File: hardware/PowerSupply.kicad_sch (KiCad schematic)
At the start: 34 parts, among them J3 VIN+, J4 GND, Q1 RevPol, U2 LM5050-1, U3 PTPS16890VMAR, U4 LMR38020FSDDAR, U5 NCP1117ST33T3G

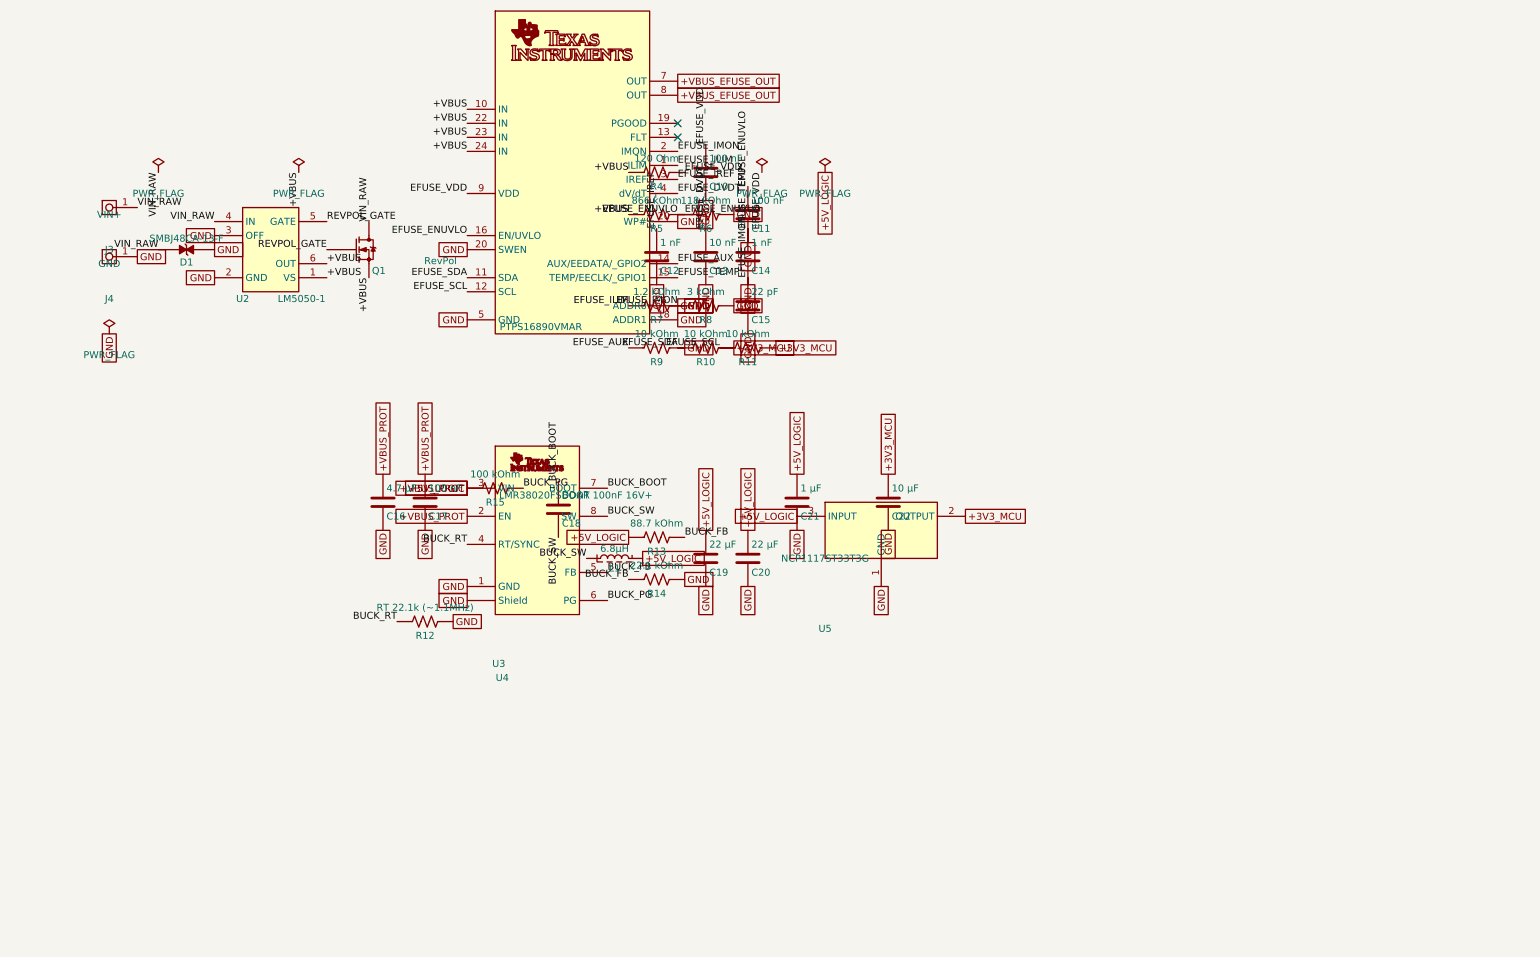
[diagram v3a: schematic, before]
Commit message: Schematic Rev B: full rebuild per METU PowerLab rules
Rev A was withdrawn: labels stuck on pins created real net shorts
(+5V_LOGIC with the 36 V bus, INHA and EFUSE_IMON with GND) and several
circuits contradicted their datasheets.

Rev B: real wires and power symbols on the 2.54 mm grid, hierarchical sheets
(half bridge reused 3x), library values, LAYOUT notes, root page with specs
and block diagram. Circuit fixes: DRV8323 VREF driven, unused buck tied to
GND, INA240A1, LM74700-Q1 reverse polarity, SMBJ36CA, eFuse per datasheet,
direct 3.3 V buck, 4.7 uH/8.1 A inductor, 2512 shunts with net-tie Kelvin,
24 V CAN ESD. kicad-cli ERC: 0 errors; netlist matches intent on all nets.
Old board and project-local library tables removed (board is rebuilt next).

Co-Authored-By: Claude Opus 5.5 <noreply@anthropic.com>
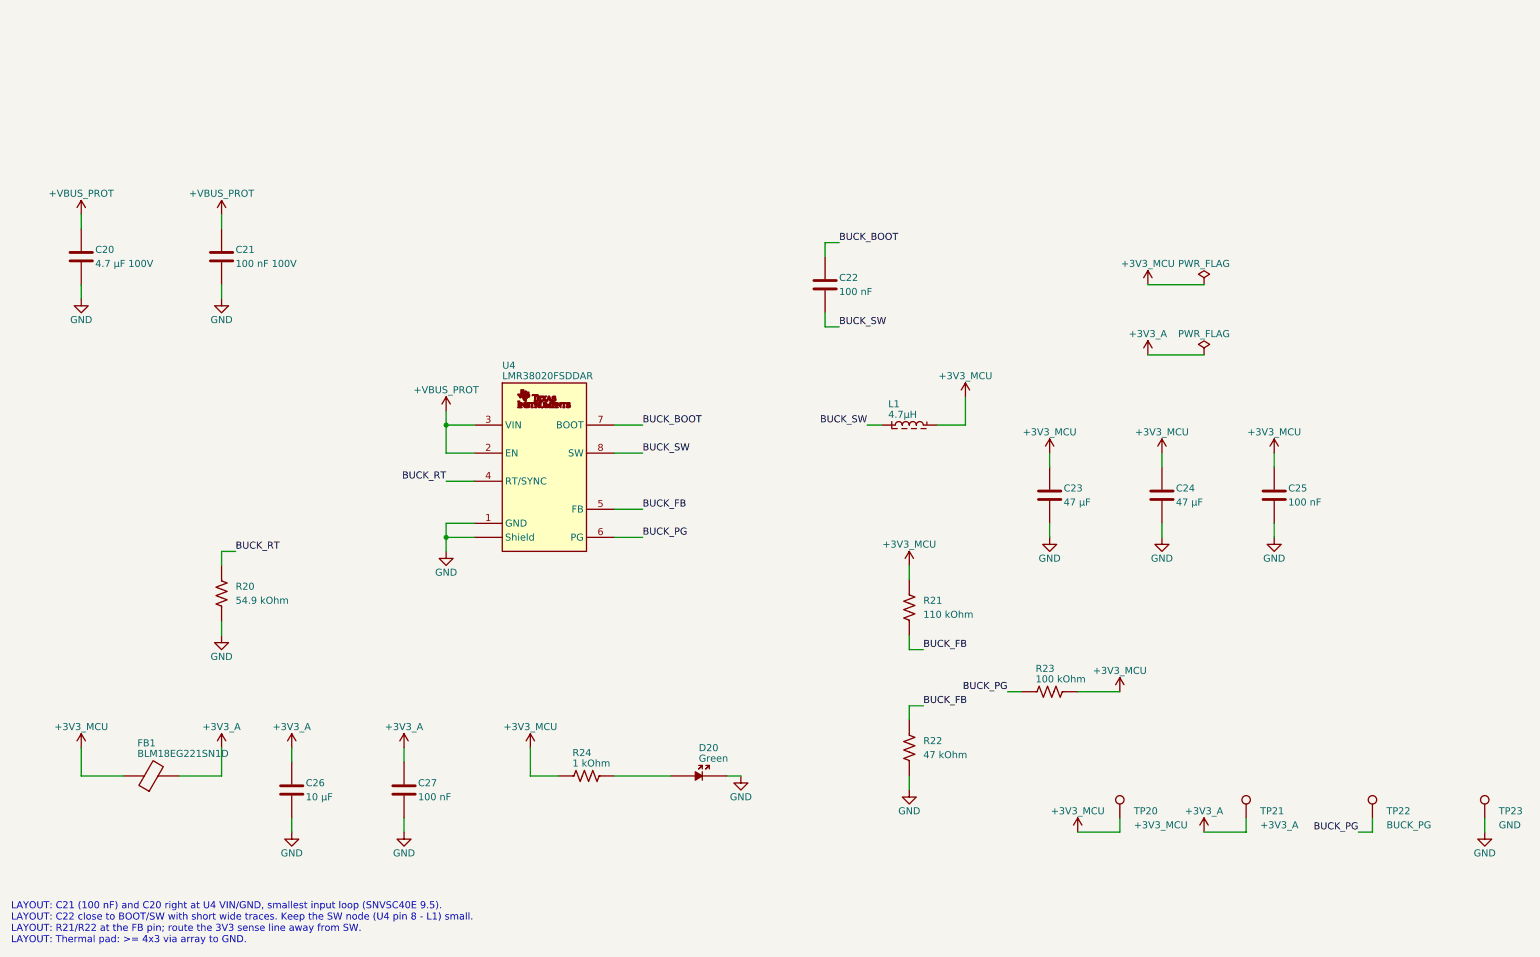
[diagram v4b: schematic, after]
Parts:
- removed C10, C11, C17: 100 nF, METUPowerLab_Capacitors_Ceramics_SurfaceMounts:0603_Medium, symbol METUPowerLab_Capacitors_Ceramics_SurfaceMounts:100 nF
- removed C12, C14: 1 nF, METUPowerLab_Capacitors_Ceramics_SurfaceMounts:0603_Medium, symbol METUPowerLab_Capacitors_Ceramics_SurfaceMounts:1 nF
- removed C13: 10 nF, METUPowerLab_Capacitors_Ceramics_SurfaceMounts:0603_Medium, symbol METUPowerLab_Capacitors_Ceramics_SurfaceMounts:10 nF
- removed C15: 22 pF, METUPowerLab_Capacitors_Ceramics_SurfaceMounts:0603_Medium, symbol METUPowerLab_Capacitors_Ceramics_SurfaceMounts:22 pF
- removed C16: 4.7 µF, METUPowerLab_Capacitors_Ceramics_SurfaceMounts:0805_Medium, symbol METUPowerLab_Capacitors_Ceramics_SurfaceMounts:4.7 µF
- removed C18: BOOT 100nF 16V+, METUPowerLab_Capacitors_Ceramics_SurfaceMounts:0603_Medium, symbol METUPowerLab_Capacitors_Ceramics_SurfaceMounts:100 nF
- removed C19, C20: 22 µF, METUPowerLab_Capacitors_Ceramics_SurfaceMounts:1210_Medium, symbol METUPowerLab_Capacitors_Ceramics_SurfaceMounts:22 µF
- removed C21: 1 µF, METUPowerLab_Capacitors_Ceramics_SurfaceMounts:0603_Medium, symbol METUPowerLab_Capacitors_Ceramics_SurfaceMounts:1 µF
- removed C22: 10 µF, METUPowerLab_Capacitors_Ceramics_SurfaceMounts:0805_Medium, symbol METUPowerLab_Capacitors_Ceramics_SurfaceMounts:10 µF
- removed D1: SMBJ48CA-13-F, METUPowerLab_Diodes_TVSDiodes:DO-214AA, symbol METUPowerLab_Diodes_TVSDiodes:SMBJ48CA-13-F
- removed J3: VIN+, METUPowerLab_Connectors_ScrewTerminals:7770, symbol METUPowerLab_Connectors_ScrewTerminals:7770
- removed J4: GND, METUPowerLab_Connectors_ScrewTerminals:7770, symbol METUPowerLab_Connectors_ScrewTerminals:7770
- removed L1: 6.8µH, METUPowerLab_Inductors_SurfaceMounts:6x6mm, symbol METUPowerLab_Inductors_SurfaceMounts:6.8µH
- removed Q1: RevPol, METUPowerLab_Transistors_MOSFETs:8-PowerTDFN(5x6mm), symbol METUPowerLab_Transistors_MOSFETs:NTMFS006N08MC
- removed R10, R11, R9: 10 kOhm, METUPowerLab_Resistors_ChipResistors:0603_Medium, symbol METUPowerLab_Resistors_ChipResistors:10 kOhm
- removed R12: RT 22.1k (~1.1MHz), METUPowerLab_Resistors_ChipResistors:0603_Medium, symbol METUPowerLab_Resistors_ChipResistors:22.1 kOhm
- removed R13: 88.7 kOhm, METUPowerLab_Resistors_ChipResistors:0603_Medium, symbol METUPowerLab_Resistors_ChipResistors:88.7 kOhm
- removed R14: 22.1 kOhm, METUPowerLab_Resistors_ChipResistors:0603_Medium, symbol METUPowerLab_Resistors_ChipResistors:22.1 kOhm
- removed R15: 100 kOhm, METUPowerLab_Resistors_ChipResistors:0603_Medium, symbol METUPowerLab_Resistors_ChipResistors:100 kOhm
- removed R4: 120 Ohm, METUPowerLab_Resistors_ChipResistors:0603_Medium, symbol METUPowerLab_Resistors_ChipResistors:120 Ohm
- removed R5: 866 kOhm, METUPowerLab_Resistors_ChipResistors:0603_Medium, symbol METUPowerLab_Resistors_ChipResistors:866 kOhm
- removed R6: 118 kOhm, METUPowerLab_Resistors_ChipResistors:0603_Medium, symbol METUPowerLab_Resistors_ChipResistors:118 kOhm
- removed R7: 1.2 kOhm, METUPowerLab_Resistors_ChipResistors:0603_Medium, symbol METUPowerLab_Resistors_ChipResistors:1.2 kOhm
- removed R8: 3 kOhm, METUPowerLab_Resistors_ChipResistors:0603_Medium, symbol METUPowerLab_Resistors_ChipResistors:3 kOhm
- removed U2: LM5050-1, METUPowerLab_CircuitProtections_IdealDiodes:SOT-23-6, symbol METUPowerLab_CircuitProtections_IdealDiodes:LM5050-1
- removed U3: PTPS16890VMAR, METUPowerLab_CircuitProtections_eFuses:23-LQFN-CLIP_(VMA), symbol METUPowerLab_CircuitProtections_eFuses:PTPS16890VMAR
- removed U5: NCP1117ST33T3G, METUPowerLab_Regulators_LDOs:SOT-223, symbol METUPowerLab_Regulators_LDOs:NCP1117ST33T3G
- added C20: 4.7 µF 100V, METUPowerLab_Capacitors_Ceramics_SurfaceMounts:1210_Medium, symbol METUPowerLab_Capacitors_Ceramics_SurfaceMounts:4.7 µF
- added C21: 100 nF 100V, METUPowerLab_Capacitors_Ceramics_SurfaceMounts:0603_Medium, symbol METUPowerLab_Capacitors_Ceramics_SurfaceMounts:100 nF 100V
- added C22, C25, C27: 100 nF, METUPowerLab_Capacitors_Ceramics_SurfaceMounts:0603_Medium, symbol METUPowerLab_Capacitors_Ceramics_SurfaceMounts:100 nF
- added C23, C24: 47 µF, METUPowerLab_Capacitors_Ceramics_SurfaceMounts:1210_Medium, symbol METUPowerLab_Capacitors_Ceramics_SurfaceMounts:47 µF
- added C26: 10 µF, METUPowerLab_Capacitors_Ceramics_SurfaceMounts:0603_Medium, symbol METUPowerLab_Capacitors_Ceramics_SurfaceMounts:10 µF
- added D20: Green, METUPowerLab_LEDs_SurfaceMounts:0603_Medium, symbol METUPowerLab_LEDs_SurfaceMounts:Green
- added FB1: BLM18EG221SN1D, METUPowerLab_CircuitProtections_FerriteBeads:0603_Medium, symbol METUPowerLab_CircuitProtections_FerriteBeads:BLM18EG221SN1D
- added L1: 4.7µH, METUPowerLab_Inductors_SurfaceMounts:6x5_7mm, symbol METUPowerLab_Inductors_SurfaceMounts:4.7µH
- added R20: 54.9 kOhm, METUPowerLab_Resistors_ChipResistors:0603_Medium, symbol METUPowerLab_Resistors_ChipResistors:54.9 kOhm
- added R21: 110 kOhm, METUPowerLab_Resistors_ChipResistors:0603_Medium, symbol METUPowerLab_Resistors_ChipResistors:110 kOhm
- added R22: 47 kOhm, METUPowerLab_Resistors_ChipResistors:0603_Medium, symbol METUPowerLab_Resistors_ChipResistors:47 kOhm
- added R23: 100 kOhm, METUPowerLab_Resistors_ChipResistors:0603_Medium, symbol METUPowerLab_Resistors_ChipResistors:100 kOhm
- added R24: 1 kOhm, METUPowerLab_Resistors_ChipResistors:0603_Medium, symbol METUPowerLab_Resistors_ChipResistors:1 kOhm
- added TP20: +3V3_MCU, METUPowerLab_TestPoints_SurfaceMounts:Pad_D1.5mm, symbol METUPowerLab_TestPoints_SurfaceMounts:TestPoint_Pad
- added TP21: +3V3_A, METUPowerLab_TestPoints_SurfaceMounts:Pad_D1.5mm, symbol METUPowerLab_TestPoints_SurfaceMounts:TestPoint_Pad
- added TP22: BUCK_PG, METUPowerLab_TestPoints_SurfaceMounts:Pad_D1.5mm, symbol METUPowerLab_TestPoints_SurfaceMounts:TestPoint_Pad
- added TP23: GND, METUPowerLab_TestPoints_SurfaceMounts:Pad_D1.5mm, symbol METUPowerLab_TestPoints_SurfaceMounts:TestPoint_Pad
- U4: Current Rating (none) -> 2A; Digi-Key Number (none) -> 296-LMR38020FSDDARCT-ND; Manufacturer (none) -> Texas Instruments; Manufacturer Number (none) -> LMR38020FSDDAR; Mounting Type (none) -> Surface Mount; Mouser Number (none) -> 595-LMR38020FSDDAR; Number of Outputs (none) -> 1; Operating Temperature (none) -> -40°C up to 150°C (TJ); Package (none) -> 8-SOICPower; Switching Frequency (none) -> 200kHz up to 2.2MHz; Synchronous Rectifier (none) -> Yes; Topology (none) -> Buck; Voltage Input Rating (none) -> 4.2V up to 80V; Voltage Output Rating (none) -> 1V up to 75V
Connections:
- net +3V3_MCU: now also C23.1, C24.1, C25.1, FB1.1, L1.2, R21.1, R23.2, R24.1, TP20.1
- net BUCK_BOOT: now also C22.1
- net BUCK_FB: now also R21.2, R22.1
- net BUCK_PG: now also R23.1, TP22.1
- net BUCK_RT: now also R20.1
- net BUCK_SW: now also C22.2, L1.1
- net GND: now also C20.2, C21.2, C23.2, C24.2, C25.2, C26.2, C27.2, D20.2, R20.2, R22.2, TP23.1
- net +5V_LOGIC renamed +VBUS_PROT
- net +VBUS_PROT: now also C20.1, C21.1
- new net: D20.1, R24.2
- new net +3V3_A: C26.1, C27.1, FB1.2, TP21.1
- no-connect marks 2 -> 0
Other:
- note added: "LAYOUT: C21 (100 nF) and C20 right at U4 VIN/GND, smallest input loop (SNVSC40E 9.5). LAYOUT: C22 close to BOOT/SW with short wide traces. Keep the SW node (U4 pin 8 - L1) small. LAYOUT: R21/R22 at the FB pin; route the 3V3 sense line away from SW. LAYOUT: Thermal pad: >= 4x3 via array to GND."
- title: ${PROJECT_NAME} -> Power Supply 3.3 V
